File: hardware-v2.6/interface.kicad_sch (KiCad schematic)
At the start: 17 parts, among them P1 TS2068_Edge, Q1 MMBT3904, SW1 NMI, SW2 TS Reset, U11 NE555

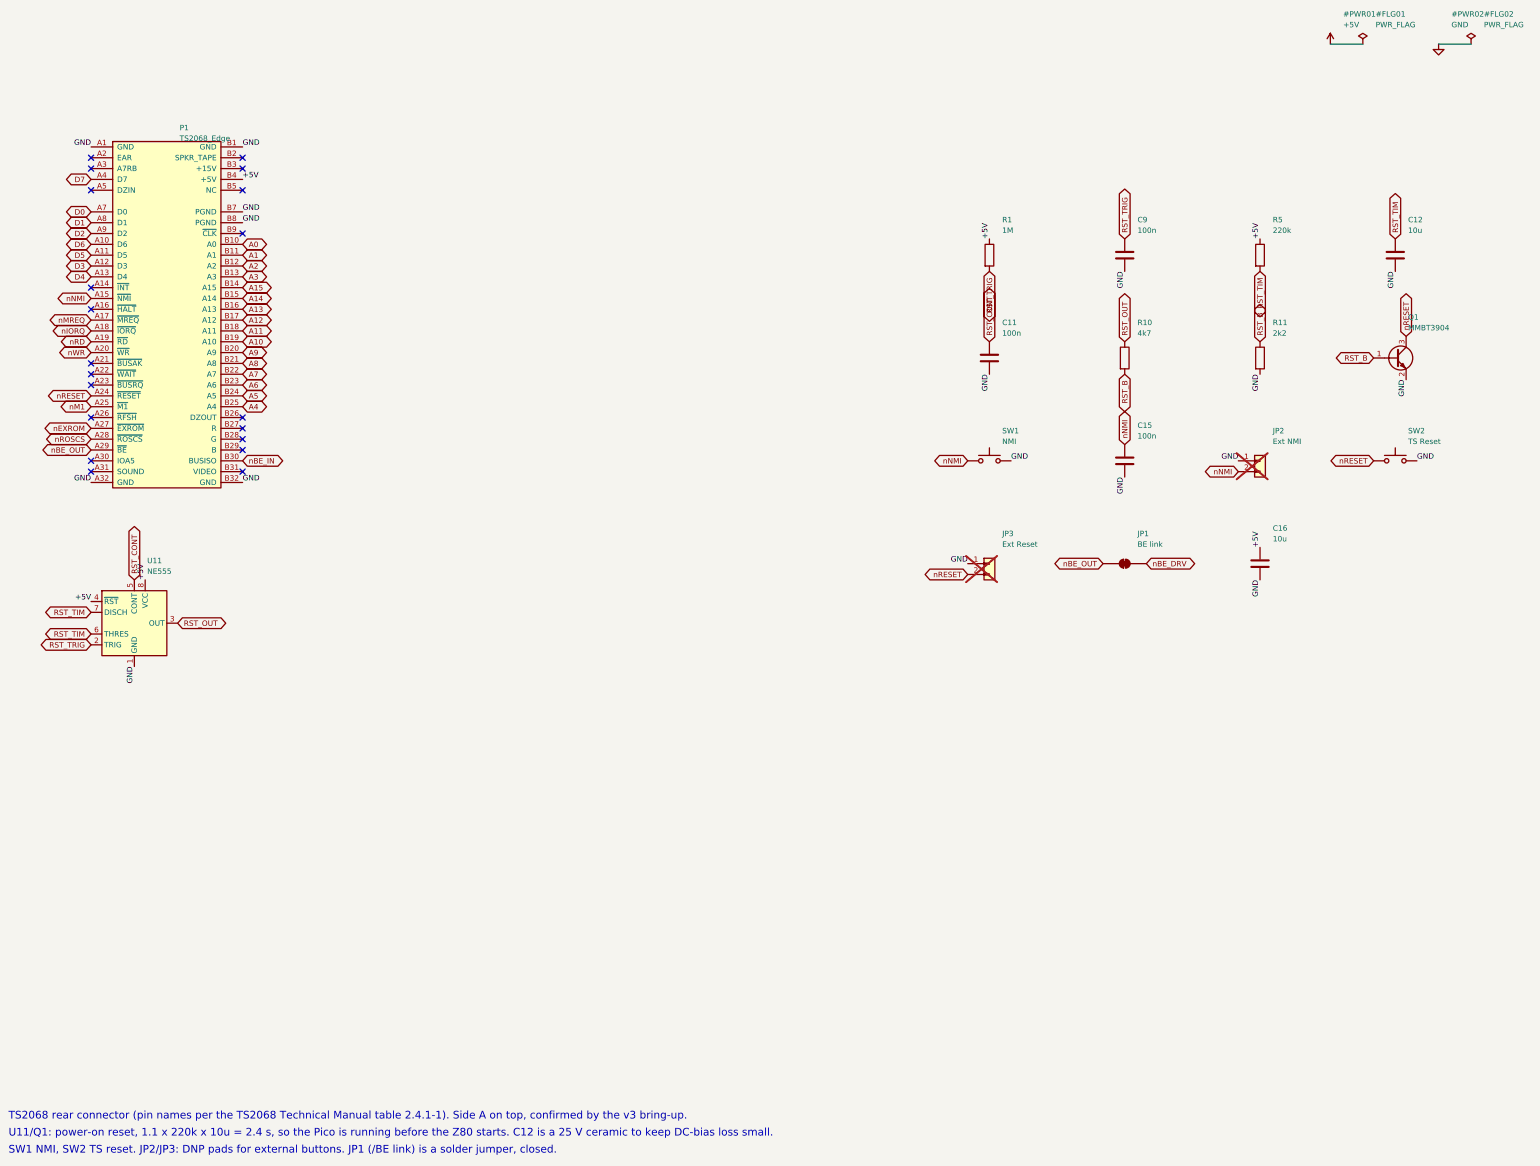
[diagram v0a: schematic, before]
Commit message: v2.6 prototype 2: glue logic in 74LVC, TPS3808 reset
The v2.2 glue (74LS04/27/32/09/157) is rebuilt in 74LVC at 3.3 V, because
the SN74LS09 (56) and XL74LS27 (108) were scarce at JLCPCB and every glue
output already ends at a 3.3 V part. Same logic at every Pico pin, so no
firmware change:

- U5 74LVC138 decodes the port (A4-A6 select; /IORQ, A7, /M1 enables);
  JP4 now picks output O0 ($00-$0F) or O1 ($10-$1F)
- U4 74LVC32: /+RW (buffered so it keeps step with /+W), /+W = /+RW-select
  OR /RD, /RDROM = A14 + A15 + /RD
- U1 74LVC1G97 (mux wired as OR with one inverted input): /MREQ_G
- U9 74LVC2G07 open-drain /BE driver; U7 channel 5 now carries /BE_IN as
  /BE_STAT, so R4 and R7 go
- U8 74LVC157 for the A14/A15 mux
- U11 TPS3808G01 replaces the 555, Q1 and passives: /RESET held below
  4.09 V and for 2.7 s after (CT 470 nF)

Checked by simulating the old and new netlists gate by gate over all
229,376 legal input states, both JP4 positions: all 12 outputs agree. The
only difference is /+W when /M1, /IORQ and /RD are all low, which a Z80
never does.

Layout: the RP2040's top/bottom-row IOVDD caps stand on their own pin's
lane with locked pin-to-cap stubs; without that the router left one net
open on three attempts. Routed first time, ERC/DRC clean at every
severity. 74 assembled parts (was 81), $9.79/board at 10.

Co-Authored-By: Claude Opus 5.5 <noreply@anthropic.com>
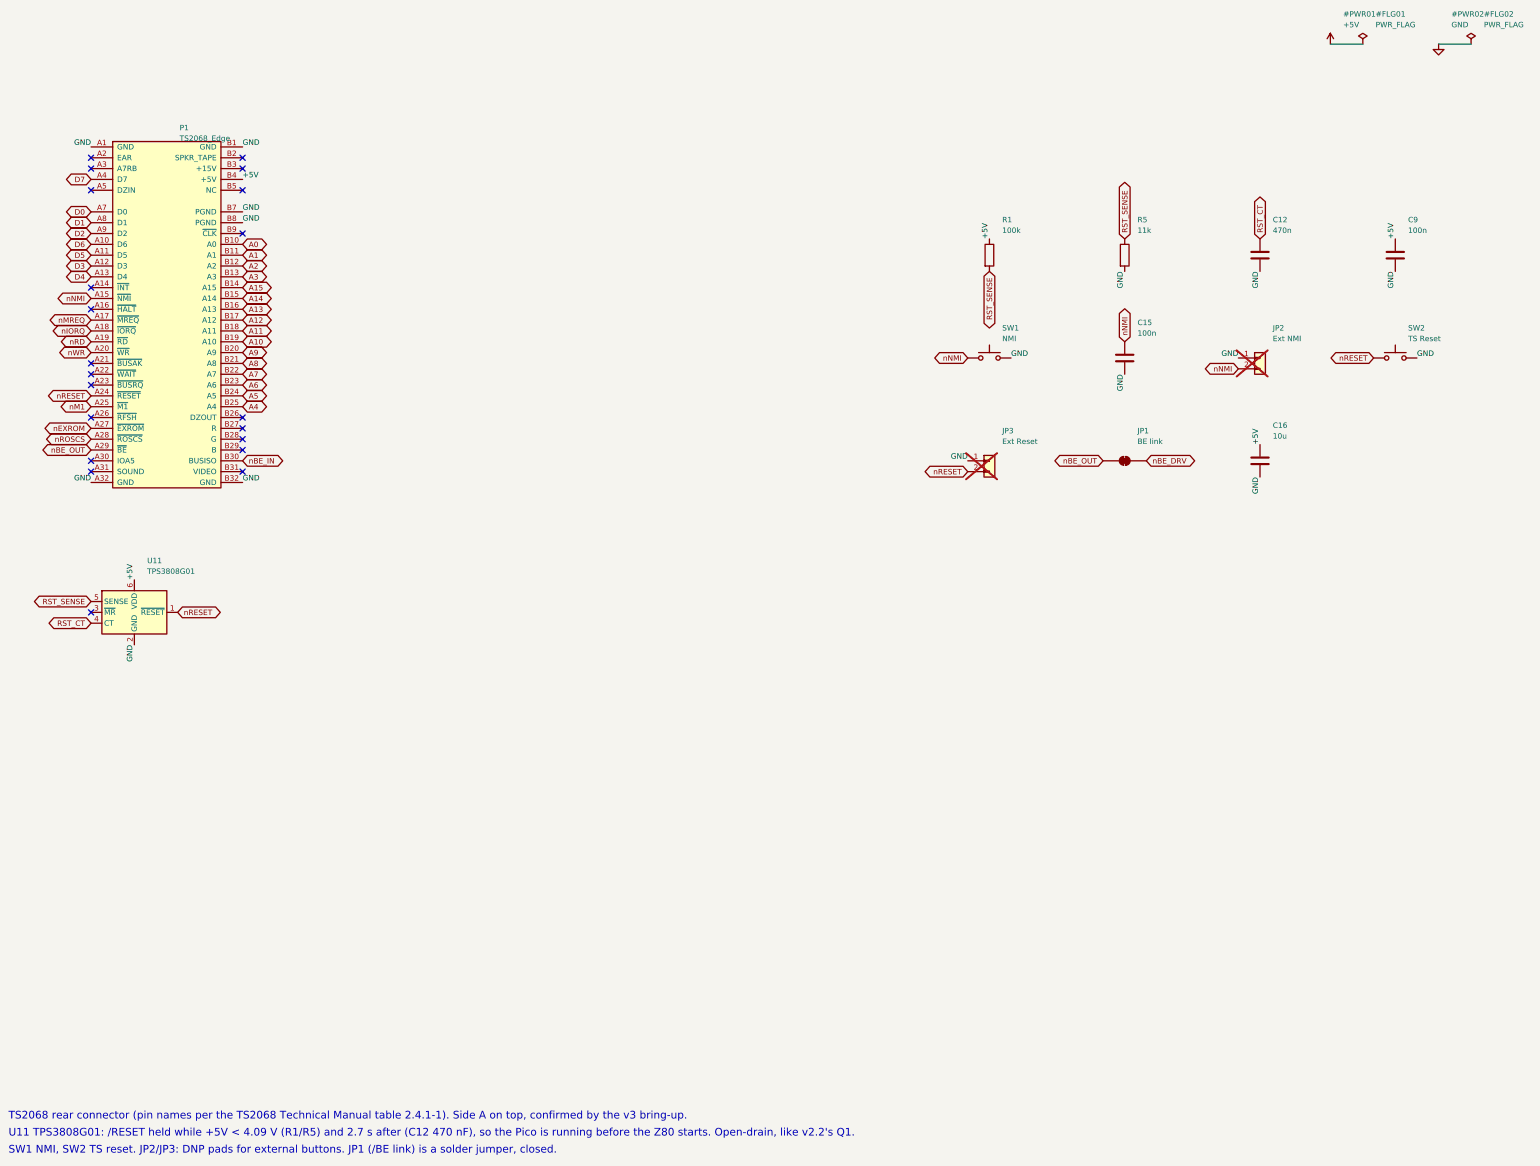
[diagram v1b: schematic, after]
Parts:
- removed C11: 100n, Capacitor_SMD:C_0603_1608Metric, symbol Device:C
- removed Q1: MMBT3904, Package_TO_SOT_SMD:SOT-23, symbol tspico:MMBT3904
- removed R10: 4k7, Resistor_SMD:R_0603_1608Metric, symbol Device:R
- removed R11: 2k2, Resistor_SMD:R_0603_1608Metric, symbol Device:R
- removed U11: NE555, Package_SO:SOIC-8_3.9x4.9mm_P1.27mm, symbol Timer:NE555D
- added U11: TPS3808G01, Package_TO_SOT_SMD:SOT-23-6, symbol Power_Supervisor:TPS3808DBV
- C12: value 10u -> 470n; footprint Capacitor_SMD:C_0805_2012Metric -> Capacitor_SMD:C_0603_1608Metric; LCSC C15850 -> C1623; MPN CL21A106KAYNNNE -> CL10B474KA8NNNC
- R1: value 1M -> 100k; LCSC C22935 -> C25803; MPN 0603WAF1004T5E -> 0603WAF1003T5E
- R5: value 220k -> 11k; LCSC C22961 -> C25950; MPN 0603WAF2203T5E -> 0603WAF1102T5E
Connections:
- net +5V: now also C9.1, U11.6 (VDD); no longer R5.1
- net GND: now also R5.2, U11.2 (GND)
- net nRESET: now also U11.1 (~{RESET})
- net RST_TIM renamed RST_CT
- net RST_CT: now also U11.4 (CT); no longer R5.2
- net RST_TRIG renamed RST_SENSE
- net RST_SENSE: now also R5.1, U11.5 (SENSE); no longer C9.1
- no-connect marks 20 -> 21
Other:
- note added: "U11 TPS3808G01: /RESET held while +5V < 4.09 V (R1/R5) and 2.7 s after (C12 470 nF), so the Pico is running before the Z80 starts. Open-drain, like v2.2's Q1."
- note removed: "U11/Q1: power-on reset, 1.1 x 220k x 10u = 2.4 s, so the Pico is running before the Z80 starts. C12 is a 25 V ceramic to keep DC-bias loss small."
